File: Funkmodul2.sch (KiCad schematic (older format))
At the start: 56 parts, among them Q10 AO3414, Q18 AO3414, Q9 SSM3J334RLFTR-ND, U6 MC74HC4538A, U7 MAX892, U8 ATMEGA128-16AU, Y2 Crystal_GND24

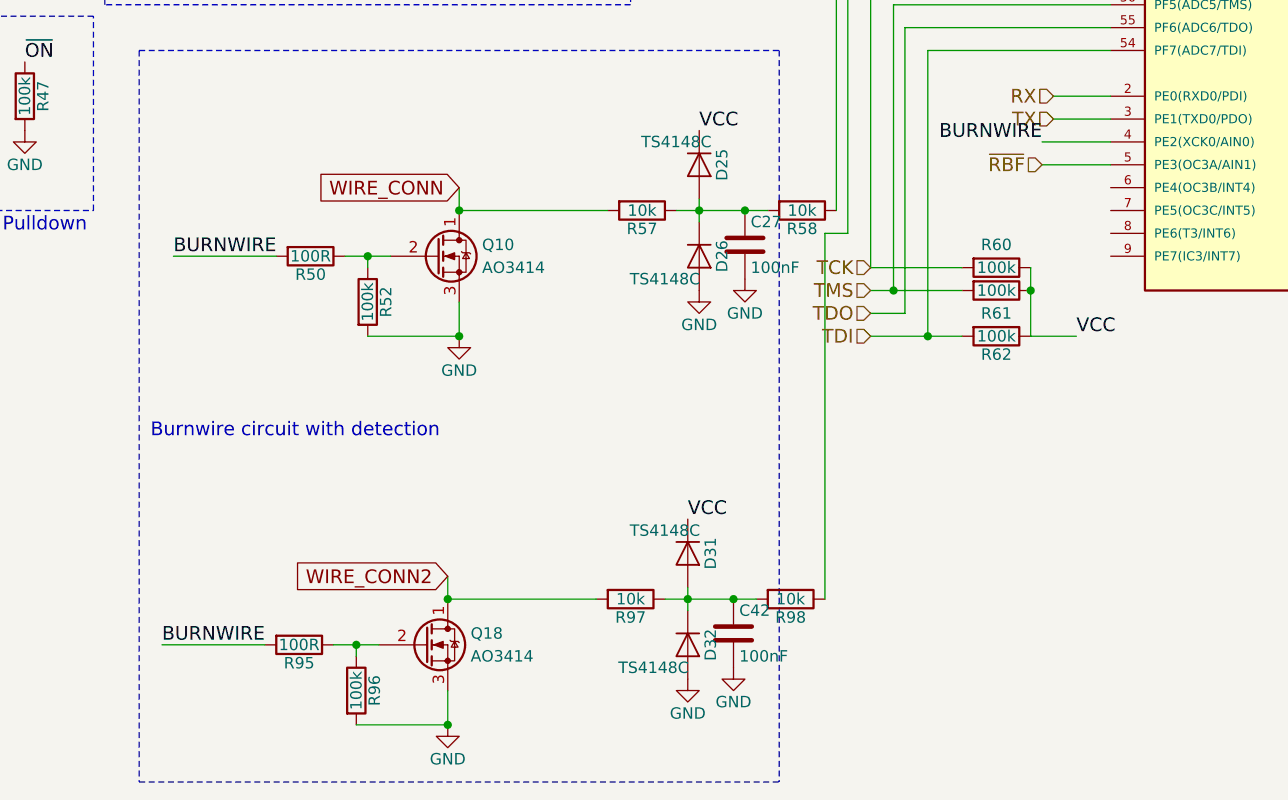
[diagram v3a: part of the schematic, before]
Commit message: Adds second burnwire fets
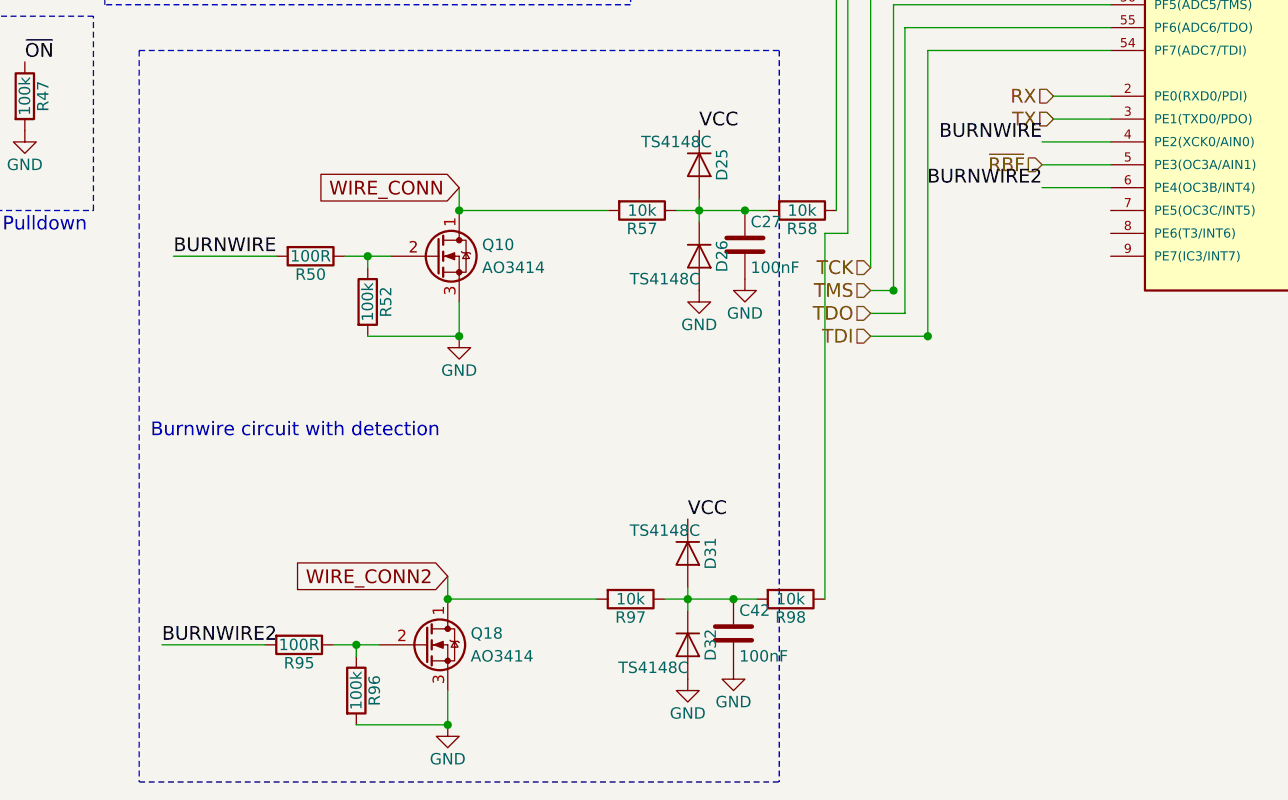
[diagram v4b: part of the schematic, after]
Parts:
- removed R60, R61, R62: 100k, Resistors_SMD:R_0603_HandSoldering, symbol R
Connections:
- net BURNWIRE: no longer R95.2
- net BURNWIRE2: now reaches U8.6 (PE4(OC3B/INT4))
- net BURNWIRE2: now also R95.2
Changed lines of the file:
@@
 $EndComp
 $Comp
-L GND #PWR61
+L GND #PWR051
 U 1 1 59B7E482
 P 3200 1650
-F 0 "#PWR61" H 3200 1400 50  0001 C CNN
+F 0 "#PWR051" H 3200 1400 50  0001 C CNN
 F 1 "GND" H 3200 1500 50  0000 C CNN
 F 2 "" H 3200 1650 50  0001 C CNN
@@
 $EndComp
 $Comp
-L GND #PWR56
+L GND #PWR052
 U 1 1 59FF9D56
 P 2250 1350
-F 0 "#PWR56" H 2250 1100 50  0001 C CNN
+F 0 "#PWR052" H 2250 1100 50  0001 C CNN
 F 1 "GND" H 2250 1200 50  0000 C CNN
 F 2 "" H 2250 1350 50  0001 C CNN
@@
 VCC
 $Comp
-L GND #PWR64
+L GND #PWR053
 U 1 1 59FF9D57
 P 3750 2450
-F 0 "#PWR64" H 3750 2200 50  0001 C CNN
+F 0 "#PWR053" H 3750 2200 50  0001 C CNN
 F 1 "GND" H 3750 2300 50  0000 C CNN
 F 2 "" H 3750 2450 50  0001 C CNN
@@
 $EndComp
 $Comp
-L GND #PWR65
+L GND #PWR054
 U 1 1 59FF9D58
 P 3750 2850
-F 0 "#PWR65" H 3750 2600 50  0001 C CNN
+F 0 "#PWR054" H 3750 2600 50  0001 C CNN
 F 1 "GND" H 3750 2700 50  0000 C CNN
 F 2 "" H 3750 2850 50  0001 C CNN
@@
 $EndComp
 $Comp
-L GND #PWR69
+L GND #PWR055
 U 1 1 59FF9D59
 P 4300 3350
-F 0 "#PWR69" H 4300 3100 50  0001 C CNN
+F 0 "#PWR055" H 4300 3100 50  0001 C CNN
 F 1 "GND" H 4300 3200 50  0000 C CNN
 F 2 "" H 4300 3350 50  0001 C CNN
@@
 $EndComp
 $Comp
-L GND #PWR70
+L GND #PWR056
 U 1 1 59B80EAC
 P 4550 2350
-F 0 "#PWR70" H 4550 2100 50  0001 C CNN
+F 0 "#PWR056" H 4550 2100 50  0001 C CNN
 F 1 "GND" H 4550 2200 50  0000 C CNN
 F 2 "" H 4550 2350 50  0001 C CNN
@@
 $EndComp
 $Comp
-L GND #PWR71
+L GND #PWR057
 U 1 1 59B80F3D
 P 5000 2350
-F 0 "#PWR71" H 5000 2100 50  0001 C CNN
+F 0 "#PWR057" H 5000 2100 50  0001 C CNN
 F 1 "GND" H 5000 2200 50  0000 C CNN
 F 2 "" H 5000 2350 50  0001 C CNN
@@
 $EndComp
 $Comp
-L GND #PWR76
+L GND #PWR058
 U 1 1 59B835F0
 P 7000 1100
-F 0 "#PWR76" H 7000 850 50  0001 C CNN
+F 0 "#PWR058" H 7000 850 50  0001 C CNN
 F 1 "GND" H 7000 950 50  0000 C CNN
 F 2 "" H 7000 1100 50  0001 C CNN
@@
 $EndComp
 $Comp
-L GND #PWR73
+L GND #PWR059
 U 1 1 59B83656
 P 6500 1150
-F 0 "#PWR73" H 6500 900 50  0001 C CNN
+F 0 "#PWR059" H 6500 900 50  0001 C CNN
 F 1 "GND" H 6500 1000 50  0000 C CNN
 F 2 "" H 6500 1150 50  0001 C CNN
@@
 $EndComp
 $Comp
-L GND #PWR72
+L GND #PWR060
 U 1 1 59B836BC
 P 6200 1150
-F 0 "#PWR72" H 6200 900 50  0001 C CNN
+F 0 "#PWR060" H 6200 900 50  0001 C CNN
 F 1 "GND" H 6200 1000 50  0000 C CNN
 F 2 "" H 6200 1150 50  0001 C CNN
@@
 $EndComp
 $Comp
-L GND #PWR74
+L GND #PWR061
 U 1 1 59FF9D5F
 P 6600 5700
-F 0 "#PWR74" H 6600 5450 50  0001 C CNN
+F 0 "#PWR061" H 6600 5450 50  0001 C CNN
 F 1 "GND" H 6600 5550 50  0000 C CNN
 F 2 "" H 6600 5700 50  0001 C CNN
@@
 $EndComp
 $Comp
-L GND #PWR75
+L GND #PWR062
 U 1 1 59FF9D60
 P 6700 5700
-F 0 "#PWR75" H 6700 5450 50  0001 C CNN
+F 0 "#PWR062" H 6700 5450 50  0001 C CNN
 F 1 "GND" H 6700 5550 50  0000 C CNN
 F 2 "" H 6700 5700 50  0001 C CNN
@@
 $EndComp
 $Comp
-L GND #PWR77
+L GND #PWR063
 U 1 1 59FF9D61
 P 7000 5700
-F 0 "#PWR77" H 7000 5450 50  0001 C CNN
+F 0 "#PWR063" H 7000 5450 50  0001 C CNN
 F 1 "GND" H 7000 5550 50  0000 C CNN
 F 2 "" H 7000 5700 50  0001 C CNN
@@
 $EndComp
 $Comp
-L GND #PWR54
+L GND #PWR064
 U 1 1 59FF9D65
 P 1650 2750
-F 0 "#PWR54" H 1650 2500 50  0001 C CNN
+F 0 "#PWR064" H 1650 2500 50  0001 C CNN
 F 1 "GND" H 1650 2600 50  0000 C CNN
 F 2 "" H 1650 2750 50  0001 C CNN
@@
 $EndComp
 $Comp
-L GND #PWR62
+L GND #PWR065
 U 1 1 59FF9D69
 P 3600 750
-F 0 "#PWR62" H 3600 500 50  0001 C CNN
+F 0 "#PWR065" H 3600 500 50  0001 C CNN
 F 1 "GND" H 3600 600 50  0000 C CNN
 F 2 "" H 3600 750 50  0001 C CNN
@@
 $EndComp
 $Comp
-L GND #PWR55
+L GND #PWR066
 U 1 1 59B8D515
 P 1750 750
-F 0 "#PWR55" H 1750 500 50  0001 C CNN
+F 0 "#PWR066" H 1750 500 50  0001 C CNN
 F 1 "GND" H 1750 600 50  0000 C CNN
 F 2 "" H 1750 750 50  0001 C CNN
@@
 $EndComp
 $Comp
-L GND #PWR57
+L GND #PWR067
 U 1 1 59B94F70
 P 2650 4050
-F 0 "#PWR57" H 2650 3800 50  0001 C CNN
+F 0 "#PWR067" H 2650 3800 50  0001 C CNN
 F 1 "GND" H 2650 3900 50  0000 C CNN
 F 2 "" H 2650 4050 50  0001 C CNN
@@
 $EndComp
 $Comp
-L GND #PWR50
+L GND #PWR068
 U 1 1 59C3023F
 P 600 1500
-F 0 "#PWR50" H 600 1250 50  0001 C CNN
+F 0 "#PWR068" H 600 1250 50  0001 C CNN
 F 1 "GND" H 600 1350 50  0000 C CNN
 F 2 "" H 600 1500 50  0001 C CNN
@@
 $EndComp
 $Comp
-L GND #PWR51
+L GND #PWR069
 U 1 1 59FF9D7D
 P 800 4850
-F 0 "#PWR51" H 800 4600 50  0001 C CNN
+F 0 "#PWR069" H 800 4600 50  0001 C CNN
 F 1 "GND" H 800 4700 50  0000 C CNN
 F 2 "" H 800 4850 50  0001 C CNN
@@
 $EndComp
 $Comp
-L GND #PWR60
+L GND #PWR070
 U 1 1 59FF9D81
 P 2950 3100
-F 0 "#PWR60" H 2950 2850 50  0001 C CNN
+F 0 "#PWR070" H 2950 2850 50  0001 C CNN
 F 1 "GND" H 2950 2950 50  0000 C CNN
 F 2 "" H 2950 3100 50  0001 C CNN
@@
 $EndComp
 $Comp
-L GND #PWR52
+L GND #PWR071
 U 1 1 59FF9D84
 P 1350 3400
-F 0 "#PWR52" H 1350 3150 50  0001 C CNN
+F 0 "#PWR071" H 1350 3150 50  0001 C CNN
 F 1 "GND" H 1350 3250 50  0000 C CNN
 F 2 "" H 1350 3400 50  0001 C CNN
@@
 $EndComp
 $Comp
-L GND #PWR59
+L GND #PWR072
 U 1 1 59FF9D8A
 P 2700 5750
-F 0 "#PWR59" H 2700 5500 50  0001 C CNN
+F 0 "#PWR072" H 2700 5500 50  0001 C CNN
 F 1 "GND" H 2700 5600 50  0000 C CNN
 F 2 "" H 2700 5750 50  0001 C CNN
@@
 $EndComp
 $Comp
-L GND #PWR66
+L GND #PWR073
 U 1 1 59FF9D8E
 P 3750 5550
-F 0 "#PWR66" H 3750 5300 50  0001 C CNN
+F 0 "#PWR073" H 3750 5300 50  0001 C CNN
 F 1 "GND" H 3750 5400 50  0000 C CNN
 F 2 "" H 3750 5550 50  0001 C CNN
@@
 $EndComp
 $Comp
-L GND #PWR68
+L GND #PWR074
 U 1 1 59FF9D91
 P 3950 5500
-F 0 "#PWR68" H 3950 5250 50  0001 C CNN
+F 0 "#PWR074" H 3950 5250 50  0001 C CNN
 F 1 "GND" H 3950 5350 50  0000 C CNN
 F 2 "" H 3950 5500 50  0001 C CNN
@@
 VCC
 $Comp
-L GND #PWR78
+L GND #PWR075
 U 1 1 59FF9DA5
 P 9100 1450
-F 0 "#PWR78" H 9100 1200 50  0001 C CNN
+F 0 "#PWR075" H 9100 1200 50  0001 C CNN
 F 1 "GND" H 9100 1300 50  0000 C CNN
 F 2 "" H 9100 1450 50  0001 C CNN
@@
 Text HLabel 4500 5750 0    60   Input ~ 0
 TDI
-$Comp
-L R R60
-U 1 1 59D42E26
-P 5050 5450
-F 0 "R60" V 4950 5450 50  0000 C CNN
-F 1 "100k" V 5050 5450 50  0000 C CNN
-F 2 "Resistors_SMD:R_0603_HandSoldering" V 4980 5450 50  0001 C CNN
-F 3 "" H 5050 5450 50  0001 C CNN
-	1    5050 5450
-	0    1    1    0
-$EndComp
-$Comp
-L R R61
-U 1 1 59D42F01
-P 5050 5550
-F 0 "R61" V 5150 5550 50  0000 C CNN
-F 1 "100k" V 5050 5550 50  0000 C CNN
-F 2 "Resistors_SMD:R_0603_HandSoldering" V 4980 5550 50  0001 C CNN
-F 3 "" H 5050 5550 50  0001 C CNN
-	1    5050 5550
-	0    1    1    0
-$EndComp
-$Comp
-L R R62
-U 1 1 59D43061
-P 5050 5750
-F 0 "R62" V 5130 5750 50  0000 C CNN
-F 1 "100k" V 5050 5750 50  0000 C CNN
-F 2 "Resistors_SMD:R_0603_HandSoldering" V 4980 5750 50  0001 C CNN
-F 3 "" H 5050 5750 50  0001 C CNN
-	1    5050 5750
-	0    1    1    0
-$EndComp
-Text Label 5400 5750 0    60   ~ 0
-VCC
 Text HLabel 5100 4000 0    60   Input ~ 0
 BAT_OK
@@
 $EndComp
 $Comp
-L GND #PWR53
+L GND #PWR076
 U 1 1 59DB2AE7
 P 1600 2400
-F 0 "#PWR53" H 1600 2150 50  0001 C CNN
+F 0 "#PWR076" H 1600 2150 50  0001 C CNN
 F 1 "GND" H 1600 2250 50  0000 C CNN
 F 2 "" H 1600 2400 50  0001 C CNN
@@
 	4600 4300 4600 5550
 Wire Wire Line
-	4500 5550 4900 5550
-Wire Wire Line
 	5550 4400 4650 4400
 Wire Wire Line
@@
 Wire Wire Line
 	4750 4500 4750 5750
-Wire Wire Line
-	4500 5750 4900 5750
-Wire Wire Line
-	4500 5450 4900 5450
 Connection ~ 4600 5550
 Connection ~ 4750 5750
 Wire Wire Line
 	4650 5650 4500 5650
-Wire Wire Line
-	5200 5450 5200 5750
-Wire Wire Line
-	5200 5750 5400 5750
-Connection ~ 5200 5550
 Wire Wire Line
 	5100 4000 5550 4000
@@
 $EndComp
 $Comp
-L GND #PWR58
+L GND #PWR077
 U 1 1 5A078216
 P 2650 7450
-F 0 "#PWR58" H 2650 7200 50  0001 C CNN
+F 0 "#PWR077" H 2650 7200 50  0001 C CNN
 F 1 "GND" H 2650 7300 50  0000 C CNN
 F 2 "" H 2650 7450 50  0001 C CNN
@@
 $EndComp
 Text Label 1400 7100 0    60   ~ 0
-BURNWIRE
+BURNWIRE2
 Text GLabel 2650 6800 0    60   Input ~ 0
 WIRE_CONN2
@@
 $EndComp
 $Comp
-L GND #PWR63
+L GND #PWR078
 U 1 1 5A078225
 P 3700 7250
-F 0 "#PWR63" H 3700 7000 50  0001 C CNN
+F 0 "#PWR078" H 3700 7000 50  0001 C CNN
 F 1 "GND" H 3700 7100 50  0000 C CNN
 F 2 "" H 3700 7250 50  0001 C CNN
@@
 $EndComp
 $Comp
-L GND #PWR67
+L GND #PWR079
 U 1 1 5A078241
 P 3900 7200
-F 0 "#PWR67" H 3900 6950 50  0001 C CNN
+F 0 "#PWR079" H 3900 6950 50  0001 C CNN
 F 1 "GND" H 3900 7050 50  0000 C CNN
 F 2 "" H 3900 7200 50  0001 C CNN
@@
 Wire Wire Line
 	4400 4100 5550 4100
+Wire Wire Line
+	4600 5550 4500 5550
+Wire Wire Line
+	4750 5750 4500 5750
+Text Label 5250 5100 2    60   ~ 0
+BURNWIRE2
+Wire Wire Line
+	5250 5100 5550 5100
 $EndSCHEMATC

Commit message: Adds BOM and production files
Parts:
- added R16: 0R, Resistors_SMD:R_0805_HandSoldering, symbol R
- Y2: value Crystal_GND24 -> 407F39D007M3728; footprint Crystals:Crystal_SMD_3225-4pin_3.2x2.5mm_HandSoldering -> Crystals:Crystal_SMD_7050-4pin_7.0x5.0mm
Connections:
- net ~ON~: now also R51.1, U6.10 (Q), U6.5 (B), R16.1; no longer D24.1 (K)
- net RESET_3V3: now reaches U8.29 ((ICP1)PD4)
- new net: D24.1 (K), R16.2
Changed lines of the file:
@@
 Text Label 2000 1250 0    60   ~ 0
 ~ON~
-Text Label 3000 2600 0    60   ~ 0
+Text Label 3300 2600 0    60   ~ 0
 ~ON~
 Text Label 3100 2300 0    60   ~ 0
@@
 P 3750 2650
 F 0 "Y2" H 3875 2850 50  0000 L CNN
-F 1 "Crystal_GND24" H 3875 2775 50  0000 L CNN
-F 2 "Crystals:Crystal_SMD_3225-4pin_3.2x2.5mm_HandSoldering" H 3750 2650 50  0001 C CNN
+F 1 "407F39D007M3728" H 3875 2775 50  0000 L CNN
+F 2 "Crystals:Crystal_SMD_7050-4pin_7.0x5.0mm" H 3750 2650 50  0001 C CNN
 F 3 "" H 3750 2650 50  0001 C CNN
 	1    3750 2650
@@
 Wire Wire Line
 	5250 5100 5550 5100
+Text HLabel 8150 5100 2    60   Input ~ 0
+RESET_3V3
+$Comp
+L R R16
+U 1 1 5A0FAB4F
+P 3150 2600
+F 0 "R16" V 3230 2600 50  0000 C CNN
+F 1 "0R" V 3150 2600 50  0000 C CNN
+F 2 "Resistors_SMD:R_0805_HandSoldering" V 3080 2600 50  0001 C CNN
+F 3 "" H 3150 2600 50  0001 C CNN
+	1    3150 2600
+	0    1    1    0
+$EndComp
 $EndSCHEMATC
